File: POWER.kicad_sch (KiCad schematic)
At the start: 39 parts, among them CN1 KF128L-5.08-2P, U1 XL1509-5.0, U2 B0503S-2WR3L, U3 SY8089A1AAC, U4 CH213K, U5 SY8089AAC

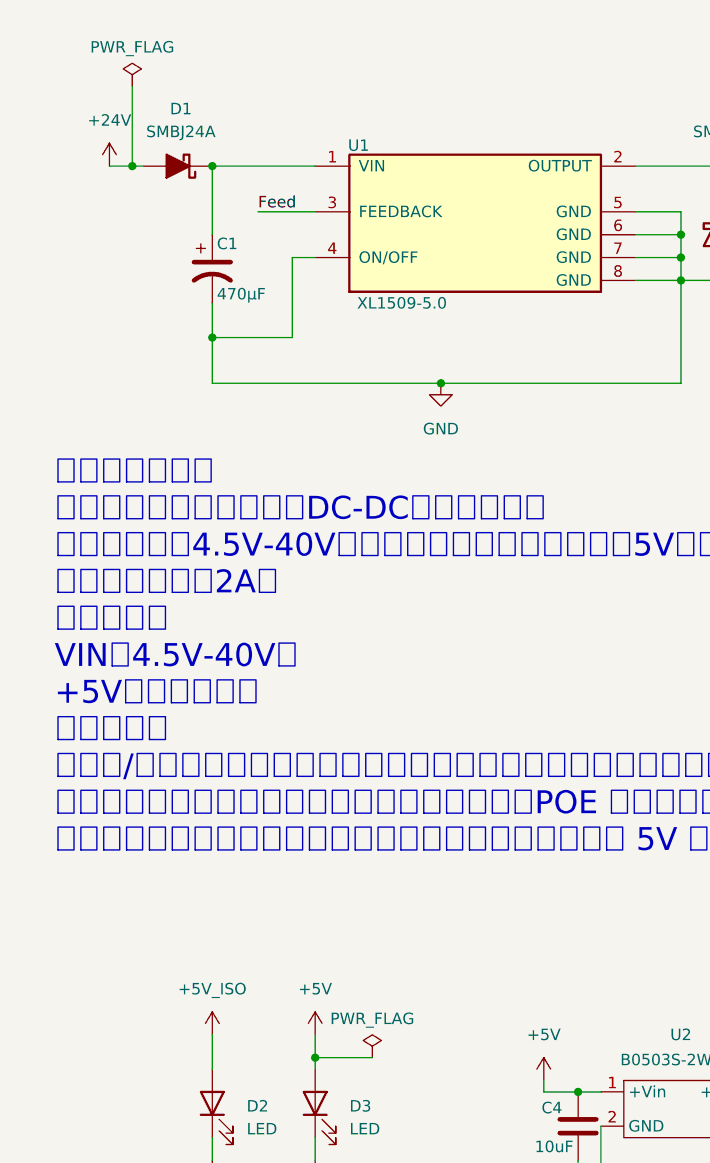
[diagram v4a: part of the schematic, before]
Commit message: 完善PCB布线与接口电源网络
- 调整控制板PCB器件布局与走线
- 更新MCU、电源及通信接口原理图
- 统一隔离接口地和电源网络标签并修正封装属性
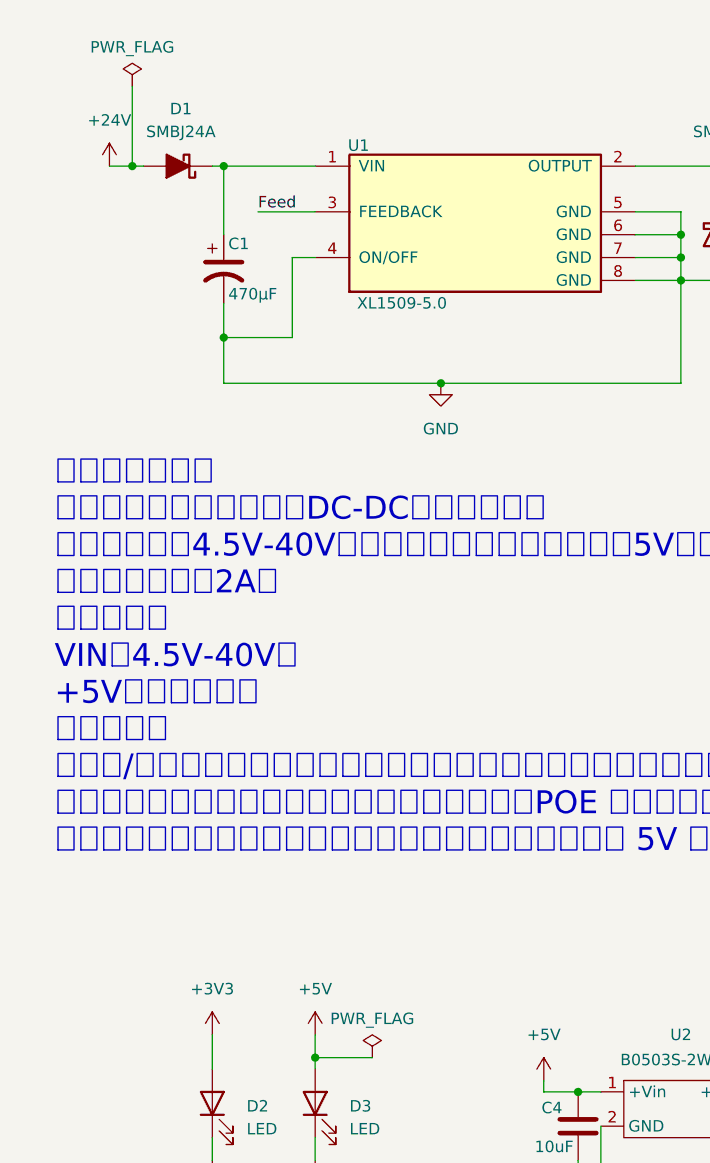
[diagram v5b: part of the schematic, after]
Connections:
- net +3V3: now also D2.2 (A)
- net +5V_ISO: no longer D2.2 (A)
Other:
- moved on the sheet: C1
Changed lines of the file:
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@@
 	)
 	(junction
-		(at 30.48 44.45)
+		(at 223.52 31.75)
 		(diameter 0)
 		(color 0 0 0 0)
 	)
 	(junction
-		(at 223.52 31.75)
+		(at 71.12 156.21)
 		(diameter 0)
 		(color 0 0 0 0)
 	)
 	(junction
-		(at 71.12 156.21)
+		(at 31.75 44.45)
 		(diameter 0)
 		(color 0 0 0 0)
@@
 	)
 	(junction
+		(at 31.75 63.5)
+		(diameter 0)
+		(color 0 0 0 0)
+	)
+	(junction
 		(at 120.65 182.88)
 		(diameter 0)
@@
 	)
 	(junction
-		(at 55.88 68.58)
+		(at 240.03 152.4)
 		(diameter 0)
 		(color 0 0 0 0)
 	)
 	(junction
-		(at 240.03 152.4)
+		(at 55.88 68.58)
 		(diameter 0)
 		(color 0 0 0 0)
@@
 	)
 	(junction
-		(at 30.48 63.5)
-		(diameter 0)
-		(color 0 0 0 0)
-	)
-	(junction
 		(at 193.04 143.51)
 		(diameter 0)
@@
 	(wire
 		(pts
-			(xy 41.91 44.45) (xy 30.48 44.45)
+			(xy 41.91 44.45) (xy 31.75 44.45)
 		)
 		(stroke
@@
 	(wire
 		(pts
+			(xy 31.75 63.5) (xy 31.75 68.58)
+		)
+		(stroke
+			(width 0)
+			(type default)
+		)
+	)
+	(wire
+		(pts
 			(xy 86.36 57.15) (xy 82.55 57.15)
 		)
@@
 	(wire
 		(pts
-			(xy 30.48 63.5) (xy 30.48 68.58)
-		)
-		(stroke
-			(width 0)
-			(type default)
-		)
-	)
-	(wire
-		(pts
 			(xy 185.42 142.24) (xy 193.04 142.24)
 		)
@@
 	(wire
 		(pts
-			(xy 55.88 68.58) (xy 30.48 68.58)
+			(xy 55.88 68.58) (xy 31.75 68.58)
 		)
 		(stroke
@@
 	(wire
 		(pts
-			(xy 30.48 59.69) (xy 30.48 63.5)
-		)
-		(stroke
-			(width 0)
-			(type default)
-		)
-	)
-	(wire
-		(pts
 			(xy 151.13 27.94) (xy 151.13 31.75)
 		)
@@
 	(wire
 		(pts
-			(xy 66.04 179.07) (xy 74.93 179.07)
+			(xy 31.75 52.07) (xy 31.75 44.45)
 		)
 		(stroke
@@
 	(wire
 		(pts
-			(xy 91.44 179.07) (xy 91.44 182.88)
+			(xy 66.04 179.07) (xy 74.93 179.07)
 		)
 		(stroke
@@
 	(wire
 		(pts
-			(xy 30.48 44.45) (xy 30.48 52.07)
+			(xy 91.44 179.07) (xy 91.44 182.88)
 		)
 		(stroke
@@
 	(wire
 		(pts
-			(xy 39.37 63.5) (xy 30.48 63.5)
+			(xy 39.37 63.5) (xy 31.75 63.5)
 		)
 		(stroke
@@
 	(wire
 		(pts
+			(xy 31.75 44.45) (xy 30.48 44.45)
+		)
+		(stroke
+			(width 0)
+			(type default)
+		)
+	)
+	(wire
+		(pts
 			(xy 49.53 166.37) (xy 41.91 166.37)
 		)
@@
 		)
 	)
+	(wire
+		(pts
+			(xy 31.75 59.69) (xy 31.75 63.5)
+		)
+		(stroke
+			(width 0)
+			(type default)
+		)
+	)
 	(image
 		(at 224.04 93.98)
@@
 		(lib_name "RVT1E471M0810_1")
 		(lib_id "RVT1E471M0810:RVT1E471M0810")
-		(at 30.48 57.15 0)
+		(at 31.75 57.15 0)
 		(unit 1)
 		(body_style 1)
@@
 		(dnp no)
 		(property "Reference" "C1"
-			(at 30.988 53.086 0)
+			(at 32.258 53.086 0)
 			(show_name no)
 			(do_not_autoplace no)
@@
 		)
 		(property "Value" "470µF"
-			(at 30.988 58.674 0)
+			(at 32.258 58.674 0)
 			(show_name no)
 			(do_not_autoplace no)
@@
 		)
 		(property "Footprint" "Capacitor_SMD:CP_Elec_10x10.5"
-			(at 30.48 57.15 0)
+			(at 31.75 57.15 0)
 			(hide yes)
 			(show_name no)
@@
 		)
 		(property "Datasheet" "http://file.elecfans.com/web2/M00/22/BF/pYYBAGGogrCAVRG2AA7jMVy9gGE112.pdf?RVT-VT_HONOR"
-			(at 30.48 57.15 0)
+			(at 31.75 57.15 0)
 			(hide yes)
 			(show_name no)
@@
 		)
 		(property "Description" "SMD Aluminum Electrolytic Capacitor AEC_D8X10.2MM_SM 470µF ±20% 25V Ф8.00 x 10.20mm 2000Hrs@105℃ 280mA"
-			(at 30.48 57.15 0)
+			(at 31.75 57.15 0)
 			(hide yes)
 			(show_name no)
@@
 		)
 		(property "MPN" "RVT1E471M0810"
-			(at 30.48 57.15 0)
+			(at 31.75 57.15 0)
 			(hide yes)
 			(show_name no)
@@
 		)
 		(property "Manufacturer" "HONOR"
-			(at 30.48 57.15 0)
+			(at 31.75 57.15 0)
 			(hide yes)
 			(show_name no)
@@
 		)
 		(property "characteristic" "Original"
-			(at 30.48 57.15 0)
+			(at 31.75 57.15 0)
 			(hide yes)
 			(show_name no)
@@
 		)
 		(property "huaqiu_pn" "G4630692"
-			(at 30.48 57.15 0)
+			(at 31.75 57.15 0)
 			(hide yes)
 			(show_name no)
@@
 		)
 		(property "lead_free" "Yes"
-			(at 30.48 57.15 0)
+			(at 31.75 57.15 0)
 			(hide yes)
 			(show_name no)
@@
 		)
 		(property "mount" "表面贴装"
-			(at 30.48 57.15 0)
+			(at 31.75 57.15 0)
 			(hide yes)
 			(show_name no)
@@
 		)
 		(property "package" "AEC_D8X10.2MM_SM"
-			(at 30.48 57.15 0)
+			(at 31.75 57.15 0)
 			(hide yes)
 			(show_name no)
@@
 		)
 		(property "packaging" "500pcs"
-			(at 30.48 57.15 0)
+			(at 31.75 57.15 0)
 			(hide yes)
 			(show_name no)
@@
 			)
 		)
-		(property "Value" "+5V_ISO"
+		(property "Value" "+3V3"
 			(at 30.48 135.89 0)
 			(show_name no)
@@
 			"36787dff-c477-468a-9e03-1a3b4b145c2e" "38ce2f56-570e-40c6-b757-aa47cf9dfda7"
 			"46700d3a-dc84-4f15-b007-b4113775407d" "5480400e-2c10-4d2a-b689-ad3a55651a0e"
-			"571c289e-4d86-4e89-b896-2a8a1f5b416a" "5aa61575-f0a3-4800-9395-32c5d2429cb1"
-			"5d64ec37-2fc4-4f94-be4b-edc8d2407dba" "769c80b7-574c-461d-b939-55541b3e4076"
-			"864aea4d-c010-46ba-bf76-2d4aceee47ac" "87663fc0-80f9-457e-89ee-f77716126e36"
-			"89ac511e-9bce-4b44-acc2-49be076367c4" "9877b5a2-f19d-47b7-9a55-3c680051384b"
+			"5587b970-4a96-4f8f-887b-d16e45082cd3" "571c289e-4d86-4e89-b896-2a8a1f5b416a"
+			"5aa61575-f0a3-4800-9395-32c5d2429cb1" "64aae99b-b31e-4d0f-9e7d-cb0871b1ff0d"
+			"8537205d-1650-4f73-afcd-f377457d48ad" "864aea4d-c010-46ba-bf76-2d4aceee47ac"
+			"87663fc0-80f9-457e-89ee-f77716126e36" "89ac511e-9bce-4b44-acc2-49be076367c4"
 			"a3ba6393-ba4a-4a18-ba16-b8b6de3d18d9" "a450bf52-f601-4a1a-9608-e2de2191c341"
-			"a629a46f-aa10-49da-8fa8-747a51441a02" "ad10da03-42c7-41ab-8272-4e697b611dc2"
-			"ae695cc4-6948-4d73-8632-01889eb13501" "b1cf9011-d0ae-41cf-9886-3915d25a9983"
-			"b22bfd10-6a69-4e9b-8f7e-75925597f621" "b3daacdd-d13f-4f71-8e75-45559c63763c"
-			"baf224da-49cd-45e8-9ff0-fc6de9a845ef" "c3c687f8-243e-4f7c-a8f2-2e61c4db08af"
+			"a6276723-3a38-45e9-8d7f-91f9e1a666ad" "a629a46f-aa10-49da-8fa8-747a51441a02"
+			"ad10da03-42c7-41ab-8272-4e697b611dc2" "ae695cc4-6948-4d73-8632-01889eb13501"
+			"b1cf9011-d0ae-41cf-9886-3915d25a9983" "b22bfd10-6a69-4e9b-8f7e-75925597f621"
+			"b3daacdd-d13f-4f71-8e75-45559c63763c" "baf224da-49cd-45e8-9ff0-fc6de9a845ef"
 			"cea6f413-c63a-4c6e-8bcb-0b8c4e4aead3" "d63dfb50-0603-483d-bef3-d27715a1603e"
-			"dc858717-44e7-4792-9b5e-fe85a664d09e" "e03c8444-e008-4a58-9245-32e54c84192d"
-			"e3226108-1576-4075-9c6f-3ef6ab673751" "e9cc422a-e8ef-4678-9425-2c4a87040a7f"
-			"eecc0daf-8b5d-45ac-b9d3-bb845ef75685" "f300bdc4-1080-41ac-b121-bcfd2228993b"
+			"dcae19d4-426f-40f6-b5e9-274c599d4e4e" "e3226108-1576-4075-9c6f-3ef6ab673751"
+			"e9cc422a-e8ef-4678-9425-2c4a87040a7f" "eecc0daf-8b5d-45ac-b9d3-bb845ef75685"
+			"f1c764d1-0cd8-44ec-b2ee-1ba8d768374f" "f300bdc4-1080-41ac-b121-bcfd2228993b"
 			"f37a2232-f27e-4a93-98b9-1b34d7863a5c" "fc49cb04-eb9c-440e-b65d-d9be5d9b350a"
-			"ff8701ce-2786-4762-ba69-b1e96abcd2ad"
+			"ff8701ce-2786-4762-ba69-b1e96abcd2ad" "ff909fae-c819-4eef-be49-b54e22d8454a"
 		)
 	)
